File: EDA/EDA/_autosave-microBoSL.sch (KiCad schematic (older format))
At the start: 53 parts, among them CON1 Micro_SD_Card, CON2 BARREL_JACK, J7 USB_B_Micro, SW1 SPST, U1 MCP1700T-3302E/TT, U3 MSQA6V1W5T2G, U4 74HC126, U5 FT232RQ, U6 ATmega328P-AU, U7 MCP7940N-xSN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

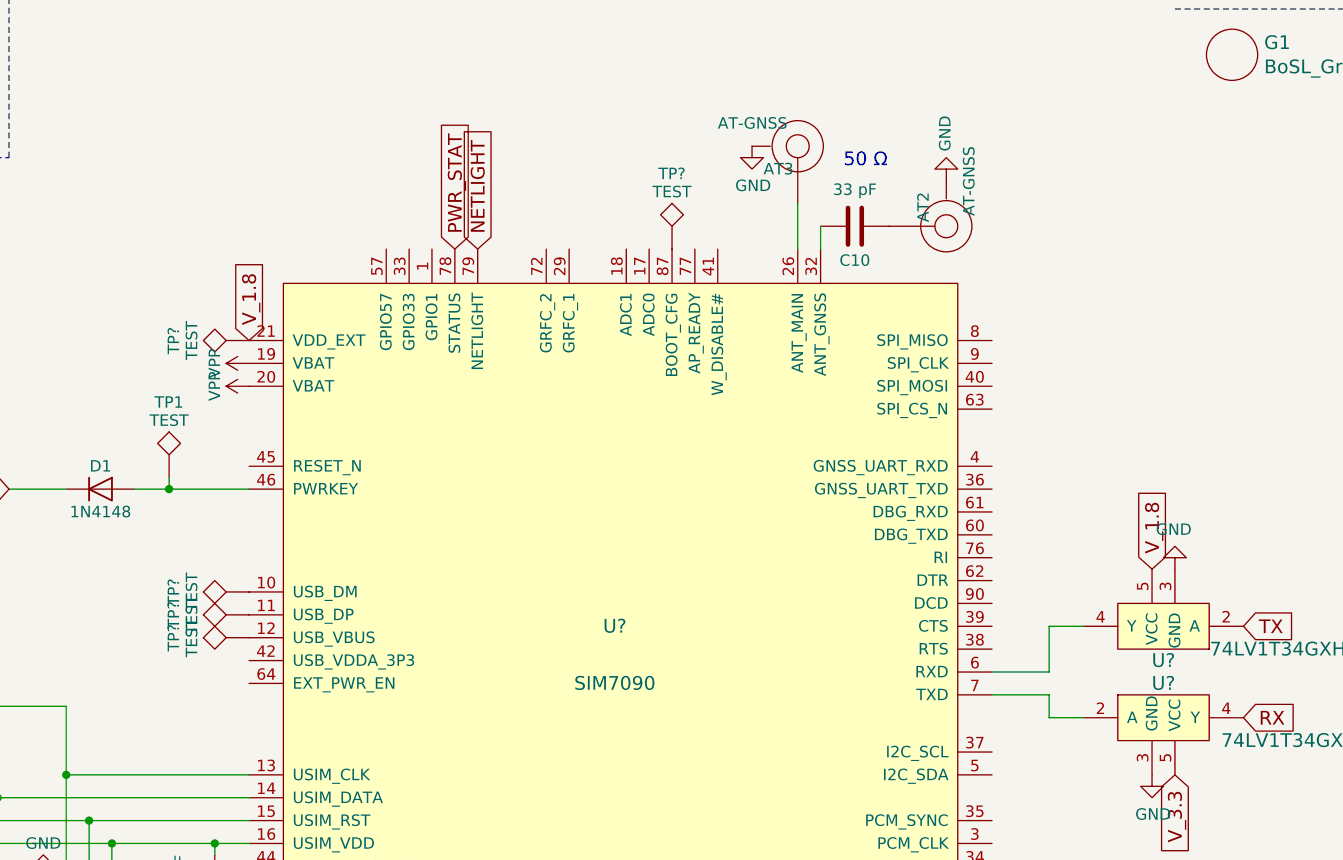
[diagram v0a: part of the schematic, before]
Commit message: added new footprints
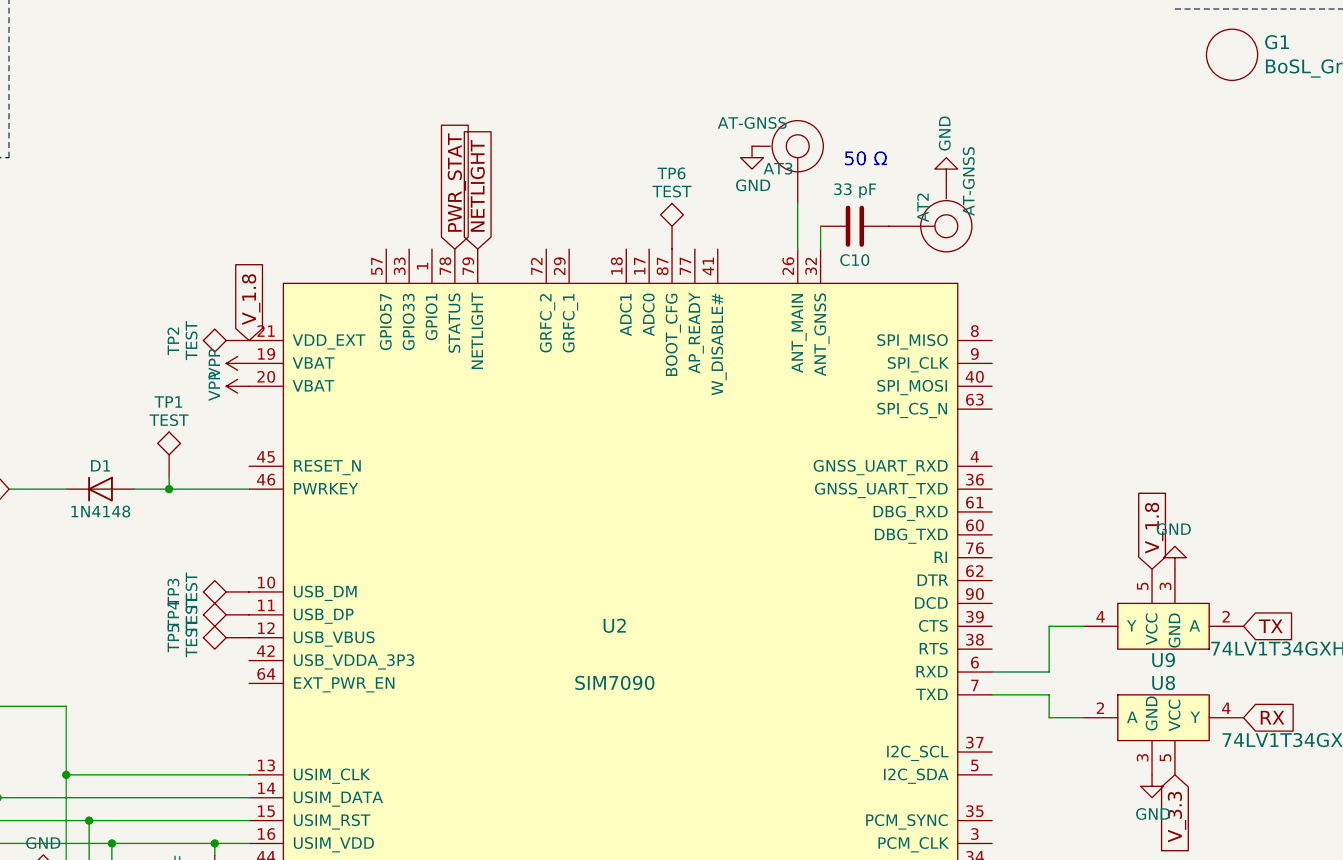
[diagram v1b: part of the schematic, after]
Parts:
- U7: footprint Package_SO:SOIC-8_3.9x4.9mm_P1.27mm -> Package_DFN_QFN:DFN-8-1EP_3x2mm_P0.5mm_EP1.3x1.5mm
- gave numbers to parts that had none: 8
